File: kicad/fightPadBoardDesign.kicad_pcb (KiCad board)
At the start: 2 copper layers, 23.9 x 3.6 mm, 30 parts

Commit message: Added layout and got the placement correct with housing
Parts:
- D1, D10, D11, D12, D13, D14, D2, D3, D4, D5, D6, D7, D8, D9: moved to B.Cu
- moved MX11 183.7 mm to (255.8, 69.0)
- moved MX12 173.2 mm to (255.8, 100.8)
- moved MX9 155.0 mm to (230.4, 62.7)
- moved MX10 154.4 mm to (230.4, 94.5)
- moved MX8 131.5 mm to (205.0, 88.1)
- moved MX7 129.3 mm to (205.0, 56.4)
- moved MX5 122.2 mm to (179.6, 62.7)
- moved D1 121.4 mm to (41.9, 75.6), turned to 90 degrees
- moved MX6 119.3 mm to (179.6, 94.5)
- moved D11 113.3 mm to (259.1, 78.4), turned to 90 degrees
- moved D9 107.1 mm to (234.3, 72.4), turned to 90 degrees
- moved D2 102.9 mm to (74.0, 66.0), turned to 90 degrees
- moved D12 101.5 mm to (257.8, 109.2)
- moved A1 92.1 mm to (247.0, 113.7), turned to -90 degrees
- moved D10 90.6 mm to (234.3, 104.4), turned to 90 degrees
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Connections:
- D3 pad 2: unconnected-(D3-A-Pad2) -> Net-(D3-A)
- MX3 pad 2: unconnected-(MX3-Pad2) -> Net-(D3-A)
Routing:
- net /Row_2: track 0.00 -> 318.7 mm
- net /Col_1: track 0.00 -> 275.5 mm, vias 0 -> 2
- net /Col_2: track 0.00 -> 246.0 mm, vias 0 -> 2
- net /Col_3: track 0.00 -> 240.2 mm, vias 0 -> 3
- net /Row_3: track 0.00 -> 166.6 mm, vias 0 -> 2
- net /Col_4: track 0.00 -> 161.6 mm, vias 0 -> 3
- net /Col_6: track 0.00 -> 142.2 mm, vias 0 -> 3
- net /Row_1: track 0.00 -> 137.8 mm, vias 0 -> 4
- net /Col_7: track 0.00 -> 124.0 mm, vias 0 -> 3
- net /Col_5: track 0.00 -> 118.5 mm, vias 0 -> 3
- net +3.3V: track 0.00 -> 109.6 mm
- net GND: track 0.00 -> 98.7 mm
- net /SCK: track 0.00 -> 77.7 mm
- net /MOSI: track 0.00 -> 72.0 mm
- net /MISO: track 0.00 -> 66.3 mm
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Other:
- board size 23.9 x 3.6 mm -> 250 x 100 mm

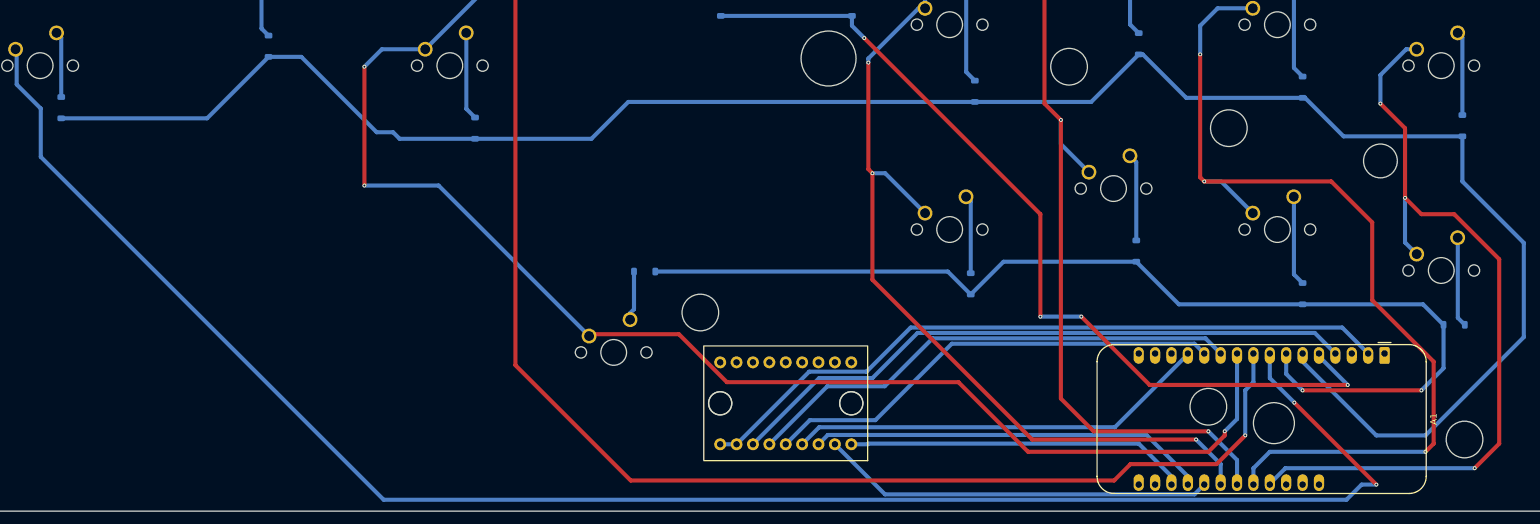
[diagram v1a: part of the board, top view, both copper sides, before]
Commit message: Updated routing and added board mount holes
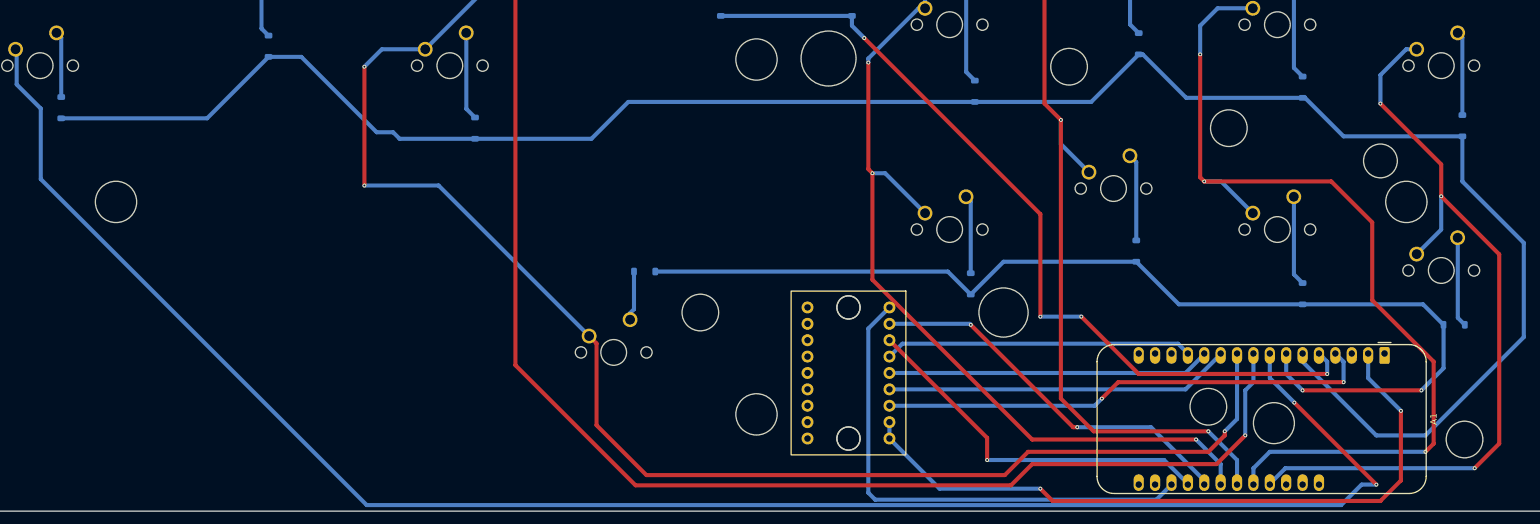
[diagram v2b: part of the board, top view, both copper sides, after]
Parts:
- moved U1 14.6 mm to (155.0, 104.0), turned to -90 degrees
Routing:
- net /TCS: track 53.0 -> 79.9 mm
- net /SCK: track 77.7 -> 53.7 mm
- net GND: track 98.7 -> 76.9 mm, vias 0 -> 2
- net /MOSI: track 72.0 -> 50.1 mm
- net /MISO: track 66.3 -> 48.5 mm
- net /Col_3: track 240.2 -> 250.8 mm
- net /Row_1: track 137.8 -> 131.3 mm
- net /DC: track 61.8 -> 58.9 mm, vias 0 -> 1
- net /Col_1: track 275.5 -> 278.2 mm
- net /Col_7: track 124.0 -> 122.1 mm
- net /RST: track 61.1 -> 59.5 mm, vias 0 -> 2
- net +3.3V: track 109.6 -> 108.9 mm, vias 0 -> 2
- net /Col_2: track 246.0 -> 246.6 mm
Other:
- outline, holes or cut-outs redrawn
